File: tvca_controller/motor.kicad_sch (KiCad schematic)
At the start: 17 parts, among them J3 4DB-P108-02, J4 PT 1,5/ 4-5,0-H, J5 4DB-P108-02, U8 VNH7070AS

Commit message: Various nit-picks
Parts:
- C4: footprint Capacitor_SMD:C_0805_2012Metric_Pad1.18x1.45mm_HandSolder -> Capacitor_THT:CP_Radial_D12.5mm_P5.00mm
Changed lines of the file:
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@@
       (effects (font (size 1.27 1.27)) (justify left))
     )
-    (property "Footprint" "Capacitor_SMD:C_0805_2012Metric_Pad1.18x1.45mm_HandSolder" (at 221.9452 52.07 0)
+    (property "Footprint" "Capacitor_THT:CP_Radial_D12.5mm_P5.00mm" (at 221.9452 52.07 0)
       (effects (font (size 1.27 1.27)) hide)
     )

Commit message: new footprint
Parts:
- F2: footprint Fuse:Fuseholder_Keystone_3555-2 -> canhw_footprints:Fuseholder_36-3557-15-ND
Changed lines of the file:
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@@
       (effects (font (size 1.27 1.27)))
     )
-    (property "Footprint" "Fuse:Fuseholder_Keystone_3555-2" (at 171.45 40.132 90)
+    (property "Footprint" "canhw_footprints:Fuseholder_36-3557-15-ND" (at 171.45 40.132 90)
       (effects (font (size 1.27 1.27)) hide)
     )

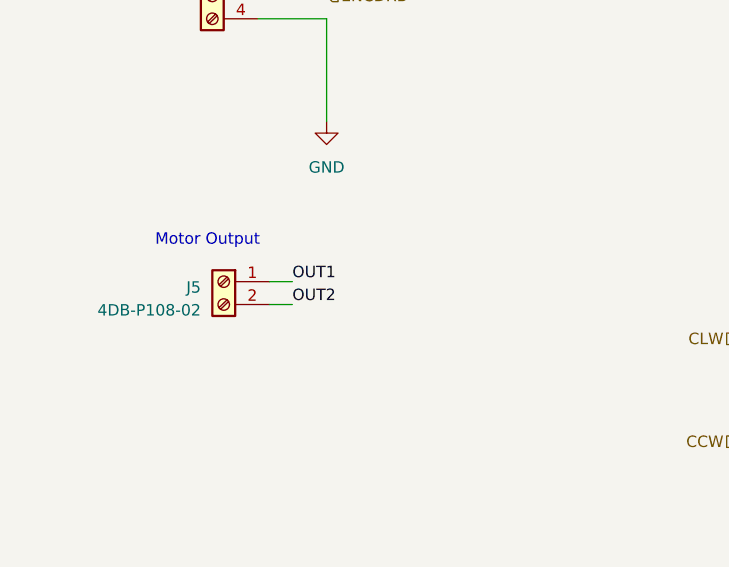
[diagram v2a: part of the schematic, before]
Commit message: Get started on PCB layout
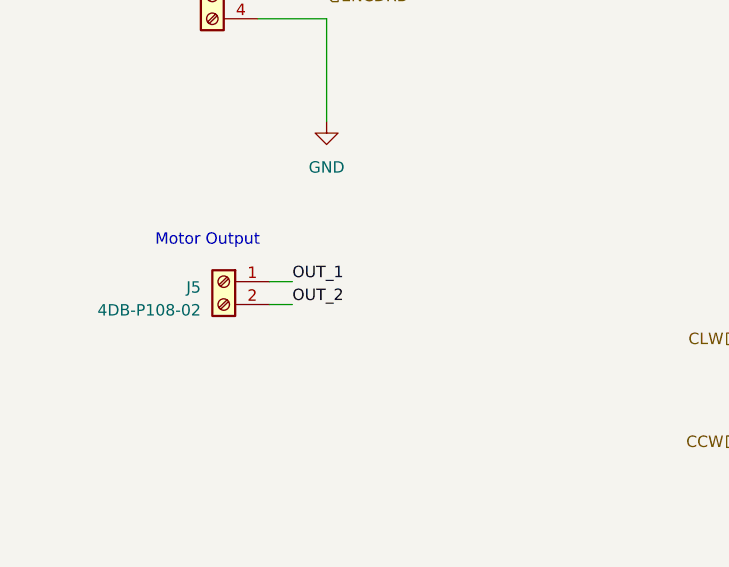
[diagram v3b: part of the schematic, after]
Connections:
- net OUT1 is gone; now on net OUT_1: J5.1 (Pin_1)
- net OUT2 is gone; now on net OUT_2: J5.2 (Pin_2)
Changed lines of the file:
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@@
     (effects (font (size 1.27 1.27)) (justify left bottom))
   )
-  (label "OUT1" (at 83.82 104.14 0) (fields_autoplaced)
+  (label "OUT_1" (at 83.82 104.14 0) (fields_autoplaced)
     (effects (font (size 1.27 1.27)) (justify left bottom))
   )
@@
     (effects (font (size 1.27 1.27)) (justify left bottom))
   )
-  (label "OUT2" (at 83.82 106.68 0) (fields_autoplaced)
+  (label "OUT_2" (at 83.82 106.68 0) (fields_autoplaced)
     (effects (font (size 1.27 1.27)) (justify left bottom))
   )

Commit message: Fix screw terminal
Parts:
- J4: footprint TerminalBlock_Phoenix:TerminalBlock_Phoenix_PT-1,5-4-5.0-H_1x04_P5.00mm_Horizontal -> TerminalBlock_Phoenix:TerminalBlock_Phoenix_MKDS-3-4-5.08_1x04_P5.08mm_Horizontal
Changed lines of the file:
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@@
       (effects (font (size 1.27 1.27)))
     )
-    (property "Footprint" "TerminalBlock_Phoenix:TerminalBlock_Phoenix_PT-1,5-4-5.0-H_1x04_P5.00mm_Horizontal" (at 74.93 69.85 0)
+    (property "Footprint" "TerminalBlock_Phoenix:TerminalBlock_Phoenix_MKDS-3-4-5.08_1x04_P5.08mm_Horizontal" (at 74.93 69.85 0)
       (effects (font (size 1.27 1.27)) hide)
     )

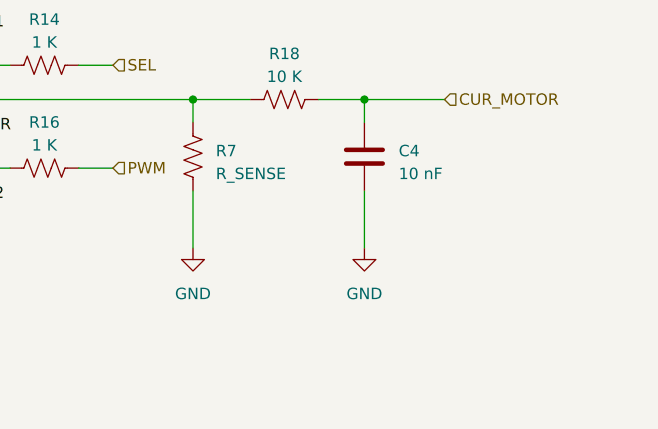
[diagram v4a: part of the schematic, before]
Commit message: Calculate R sense
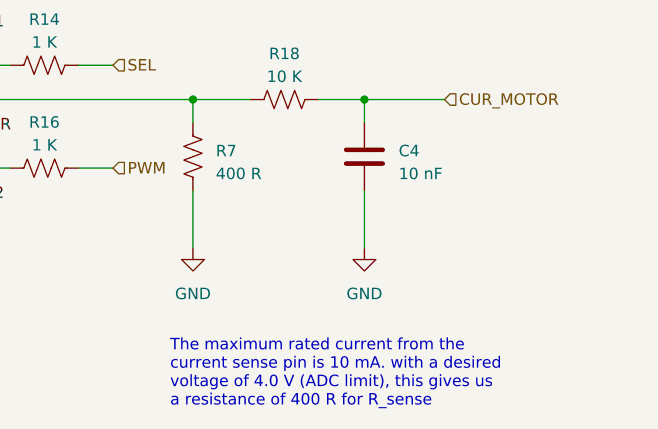
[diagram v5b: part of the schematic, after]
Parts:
- R7: value R_SENSE -> 400 R
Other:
- note added: "The maximum rated current from the current sense pin is 10 mA. with a desired voltage of 4.0 V (ADC limit), this gives us a resistance of 400 R for R_sense"
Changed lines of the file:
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@@
     (effects (font (size 1.27 1.27)) (justify right bottom))
+  )
+  (text "The maximum rated current from the \ncurrent sense pin is 10 mA. with a desired\nvoltage of 4.0 V (ADC limit), this gives us\na resistance of 400 R for R_sense\n"
+    (at 201.93 148.59 0)
+    (effects (font (size 1.27 1.27)) (justify left bottom))
   )
   (text "Motor Output\n" (at 68.58 100.33 0)
@@
       (effects (font (size 1.27 1.27)) (justify left))
     )
-    (property "Value" "R_SENSE" (at 207.01 122.555 0)
-      (effects (font (size 1.27 1.27)) (justify left))
-    )
+    (property "Value" "400 R" (at 207.01 122.555 0)
+      (effects (font (size 1.27 1.27)) (justify left))
+    )

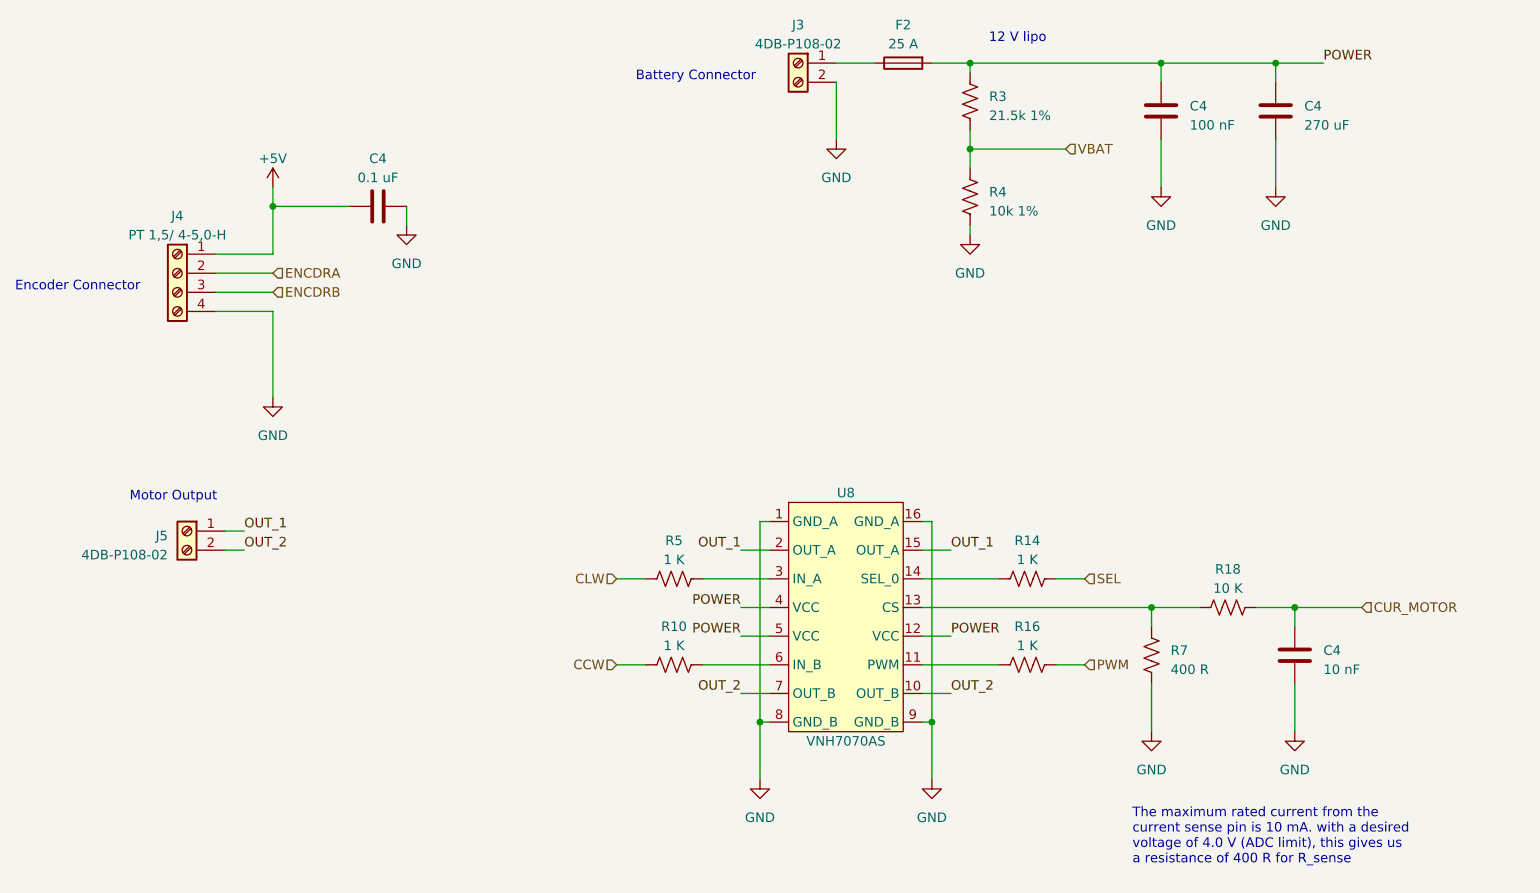
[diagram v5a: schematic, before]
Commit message: Fix units/R-sense calculation
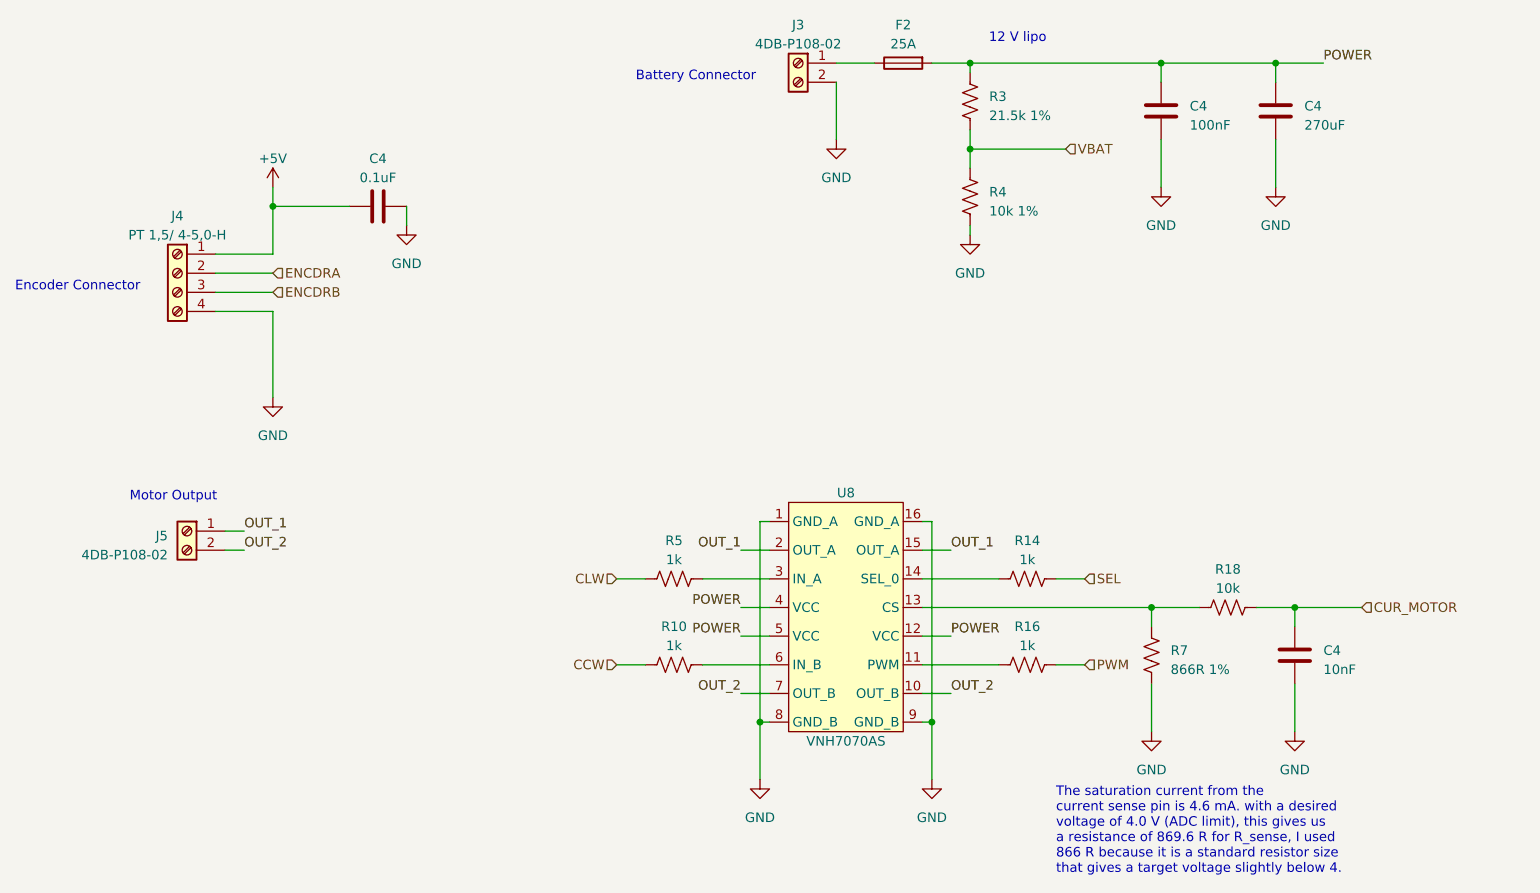
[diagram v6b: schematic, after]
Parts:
- C4: value 100 nF -> 100nF
- C4: value 10 nF -> 10nF
- C4: value 270 uF -> 270uF
- C4: value 0.1 uF -> 0.1uF
- F2: value 25 A -> 25A
- R10, R14, R16, R5: value 1 K -> 1k
- R18: value 10 K -> 10k
- R7: value 400 R -> 866R 1%
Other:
- note added: "The saturation current from the current sense pin is 4.6 mA. with a desired voltage of 4.0 V (ADC limit), this gives us a resistance of 869.6 R for R_sense, I used 866 R because it is a standard resistor size that gives a target voltage slightly below 4."
- note removed: "The maximum rated current from the current sense pin is 10 mA. with a desired voltage of 4.0 V (ADC limit), this gives us a resistance of 400 R for R_sense"
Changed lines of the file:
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@@
     (effects (font (size 1.27 1.27)) (justify right bottom))
   )
-  (text "The maximum rated current from the \ncurrent sense pin is 10 mA. with a desired\nvoltage of 4.0 V (ADC limit), this gives us\na resistance of 400 R for R_sense\n"
-    (at 201.93 148.59 0)
+  (text "The saturation current from the \ncurrent sense pin is 4.6 mA. with a desired\nvoltage of 4.0 V (ADC limit), this gives us\na resistance of 869.6 R for R_sense, I used\n866 R because it is a standard resistor size\nthat gives a target voltage slightly below 4.\n"
+    (at 191.77 149.86 0)
     (effects (font (size 1.27 1.27)) (justify left bottom))
   )
@@
       (effects (font (size 1.27 1.27)))
     )
-    (property "Value" "10 K" (at 214.63 111.76 90)
+    (property "Value" "10k" (at 214.63 111.76 90)
       (effects (font (size 1.27 1.27)))
     )
@@
       (effects (font (size 1.27 1.27)) (justify left))
     )
-    (property "Value" "100 nF" (at 209.55 50.165 0)
+    (property "Value" "100nF" (at 209.55 50.165 0)
       (effects (font (size 1.27 1.27)) (justify left))
     )
@@
       (effects (font (size 1.27 1.27)))
     )
-    (property "Value" "1 K" (at 187.96 119.38 90)
+    (property "Value" "1k" (at 187.96 119.38 90)
       (effects (font (size 1.27 1.27)))
     )
@@
       (effects (font (size 1.27 1.27)))
     )
-    (property "Value" "1 K" (at 187.96 107.95 90)
+    (property "Value" "1k" (at 187.96 107.95 90)
       (effects (font (size 1.27 1.27)))
     )
@@
       (effects (font (size 1.27 1.27)) (justify left))
     )
-    (property "Value" "400 R" (at 207.01 122.555 0)
+    (property "Value" "866R 1%" (at 207.01 122.555 0)
       (effects (font (size 1.27 1.27)) (justify left))
     )
@@
       (effects (font (size 1.27 1.27)) (justify left))
     )
-    (property "Value" "10 nF" (at 227.33 122.555 0)
+    (property "Value" "10nF" (at 227.33 122.555 0)
       (effects (font (size 1.27 1.27)) (justify left))
     )
@@
       (effects (font (size 1.27 1.27)) (justify left))
     )
-    (property "Value" "270 uF" (at 224.79 50.165 0)
+    (property "Value" "270uF" (at 224.79 50.165 0)
       (effects (font (size 1.27 1.27)) (justify left))
     )
@@
       (effects (font (size 1.27 1.27)))
     )
-    (property "Value" "0.1 uF" (at 101.6 57.15 90)
+    (property "Value" "0.1uF" (at 101.6 57.15 90)
       (effects (font (size 1.27 1.27)))
     )
@@
       (effects (font (size 1.27 1.27)))
     )
-    (property "Value" "1 K" (at 140.97 107.95 90)
+    (property "Value" "1k" (at 140.97 107.95 90)
       (effects (font (size 1.27 1.27)))
     )
@@
       (effects (font (size 1.27 1.27)))
     )
-    (property "Value" "25 A" (at 171.45 39.37 90)
+    (property "Value" "25A" (at 171.45 39.37 90)
       (effects (font (size 1.27 1.27)))
     )
@@
       (effects (font (size 1.27 1.27)))
     )
-    (property "Value" "1 K" (at 140.97 119.38 90)
-      (effects (font (size 1.27 1.27)))
-    )
+    (property "Value" "1k" (at 140.97 119.38 90)
+      (effects (font (size 1.27 1.27)))
+    )

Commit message: New PCB layout
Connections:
- net OUT_1: now also J5.2 (Pin_2); no longer J5.1 (Pin_1)
- net OUT_2: now also J5.1 (Pin_1); no longer J5.2 (Pin_2)
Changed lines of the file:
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@@
-    (stroke (width 0) (type default))
-  )
-  (wire (pts (xy 83.82 106.68) (xy 81.28 106.68))
     (stroke (width 0) (type default))
   )
@@
     (stroke (width 0) (type default))
   )
+  (wire (pts (xy 81.28 106.68) (xy 83.82 106.68))
+    (stroke (width 0) (type default))
+  )
+  (wire (pts (xy 81.28 104.14) (xy 83.82 104.14))
+    (stroke (width 0) (type default))
+  )
   (wire (pts (xy 87.63 74.93) (xy 87.63 86.36))
     (stroke (width 0) (type default))
@@
     (stroke (width 0) (type default))
   )
-  (wire (pts (xy 83.82 104.14) (xy 81.28 104.14))
-    (stroke (width 0) (type default))
-  )
   (wire (pts (xy 80.01 72.39) (xy 87.63 72.39))
     (stroke (width 0) (type default))
@@
     (effects (font (size 1.27 1.27)) (justify left bottom))
   )
-  (label "OUT_1" (at 83.82 104.14 0) (fields_autoplaced)
+  (label "OUT_1" (at 83.82 106.68 0) (fields_autoplaced)
     (effects (font (size 1.27 1.27)) (justify left bottom))
   )
@@
     (effects (font (size 1.27 1.27)) (justify left bottom))
   )
-  (label "OUT_2" (at 83.82 106.68 0) (fields_autoplaced)
+  (label "OUT_2" (at 83.82 104.14 0) (fields_autoplaced)
     (effects (font (size 1.27 1.27)) (justify left bottom))
   )

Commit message: finalize layout
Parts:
- added TP1: TestPoint, TestPoint:TestPoint_THTPad_2.5x2.5mm_Drill1.2mm, symbol Connector:TestPoint
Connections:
- net CUR_MOTOR: now also TP1.1
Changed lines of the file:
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@@
   (junction (at 180.34 41.91) (diameter 0) (color 0 0 0 0)
   )
+  (junction (at 228.6 114.3) (diameter 0) (color 0 0 0 0)
+  )
   (junction (at 205.74 41.91) (diameter 0) (color 0 0 0 0)
   )
@@
     (stroke (width 0) (type default))
   )
-  (wire (pts (xy 223.52 114.3) (xy 232.41 114.3))
+  (wire (pts (xy 223.52 114.3) (xy 228.6 114.3))
     (stroke (width 0) (type default))
   )
@@
     (stroke (width 0) (type default))
   )
+  (wire (pts (xy 228.6 106.68) (xy 228.6 114.3))
+    (stroke (width 0) (type default))
+  )
   (wire (pts (xy 223.52 124.46) (xy 223.52 130.81))
     (stroke (width 0) (type default))
@@
   )
   (wire (pts (xy 80.01 72.39) (xy 87.63 72.39))
+    (stroke (width 0) (type default))
+  )
+  (wire (pts (xy 228.6 114.3) (xy 232.41 114.3))
     (stroke (width 0) (type default))
   )
@@
       (effects (font (size 1.27 1.27)) hide)
     )
-    (property "Datasheet" "" (at 166.37 110.49 0)
+    (property "Datasheet" "https://www.st.com/content/ccc/resource/technical/document/datasheet/08/97/0a/0c/cf/4b/41/40/DM00213876.pdf/files/DM00213876.pdf/jcr:content/translations/en.DM00213876.pdf" (at 166.37 110.49 0)
       (effects (font (size 1.27 1.27)) hide)
     )
@@
         )
       )
+    )
+  )
+  (symbol (lib_id "Connector:TestPoint") (at 228.6 106.68 0) (unit 1)
+    (in_bom yes) (on_board yes) (dnp no) (fields_autoplaced)
+    (property "Reference" "TP1" (at 231.14 102.743 0)
+      (effects (font (size 1.27 1.27)) (justify left))
+    )
+    (property "Value" "TestPoint" (at 231.14 105.283 0)
+      (effects (font (size 1.27 1.27)) (justify left))
+    )
+    (property "Footprint" "TestPoint:TestPoint_THTPad_2.5x2.5mm_Drill1.2mm" (at 233.68 106.68 0)
+      (effects (font (size 1.27 1.27)) hide)
+    )
+    (property "Datasheet" "~" (at 233.68 106.68 0)
+      (effects (font (size 1.27 1.27)) hide)
+    )
+    (pin "1")
+    (instances
+      (project "tvca_controller"
+        (path "/f08602f6-65d5-48ec-b5dd-079a575e1be0/de8e002c-85d6-4a68-b910-e72b1e3d7295"
+          (reference "TP1") (unit 1)
+        )
+        (path "/f08602f6-65d5-48ec-b5dd-079a575e1be0/683c4c4a-2712-4619-b371-c4b4e0f76f26"
+          (reference "TP2") (unit 1)
+        )
+      )
